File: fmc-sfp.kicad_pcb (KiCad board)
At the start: 2 copper layers, 89.5 x 70 mm, 41 parts, among them J1 ASP-134604-01, J2 SFP+, J3 SFP+, J4 132134, J5 132134, J6 132134, J7 132134, U1 MAX9113EKA_TT, U2 MAX9113EKA_TT

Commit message: update after Phil review
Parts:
- removed J3: SFP+, Connector:Connector_SFP_and_Cage
- removed R10, R15, R16, R17, R18, R7, R8, R9: 10k, Resistor_SMD:R_0603_1608Metric
- added G***: LOGO, project:Microridge_logo, B.Cu at (118.2, 78.8)
- added J8: SFPK-SL, project:SAMTEC_SFPK-SL, B.Cu at (104.0, 60.1)
- J2: value SFP+ -> SFPK-SL; footprint Connector:Connector_SFP_and_Cage -> project:SAMTEC_SFPK-SL
- moved J2 37.5 mm to (103.7, 97.2), turned to -90 degrees
- moved J4 3.95 mm to (89.2, 54.2)
- moved J7 3.95 mm to (89.1, 109.7)
- moved J6 1.05 mm to (75.6, 109.8)
- moved J5 1.05 mm to (75.8, 54.2)
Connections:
- J2 pad 10: unconnected-(J2-VeeR-Pad10)_1 -> GND
- J2 pad 11: unconnected-(J2-VeeR-Pad10)_0 -> GND
- J2 pad 12: /lvds_0_rx_N -> /lvds_1_rx_N
- J2 pad 13: /lvds_0_rx_P -> /lvds_1_rx_P
- J2 pad 14: unconnected-(J2-VeeR-Pad10) -> GND
- J2 pad 15: unconnected-(J2-VccR-Pad15) -> /SPF1/VccR
- J2 pad 16: unconnected-(J2-VccT-Pad16) -> /SPF1/VccT
- J2 pad 17: unconnected-(J2-VeeT-Pad1)_0 -> GND
- J2 pad 18: /lvds_0_tx_P -> /lvds_1_tx_P
- J2 pad 19: /lvds_0_tx_N -> /lvds_1_tx_N
- J2 pad 20: unconnected-(J2-VeeT-Pad1)_1 -> GND
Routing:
- net VSS: track 83.2 -> 55.6 mm, vias 5 -> 4
- net GND: track 8.23 -> 15.2 mm
- net /RX0: track 16.6 -> 18.2 mm
- net /RX1: track 10.1 -> 11.7 mm
- net /lvds_0_tx_N: track 37.9 -> 36.6 mm
- net /lvds_0_tx_P: track 39.5 -> 38.1 mm
- net /lvds_1_tx_P: track 51.1 -> 49.8 mm
- net /lvds_1_tx_N: track 49.9 -> 48.5 mm

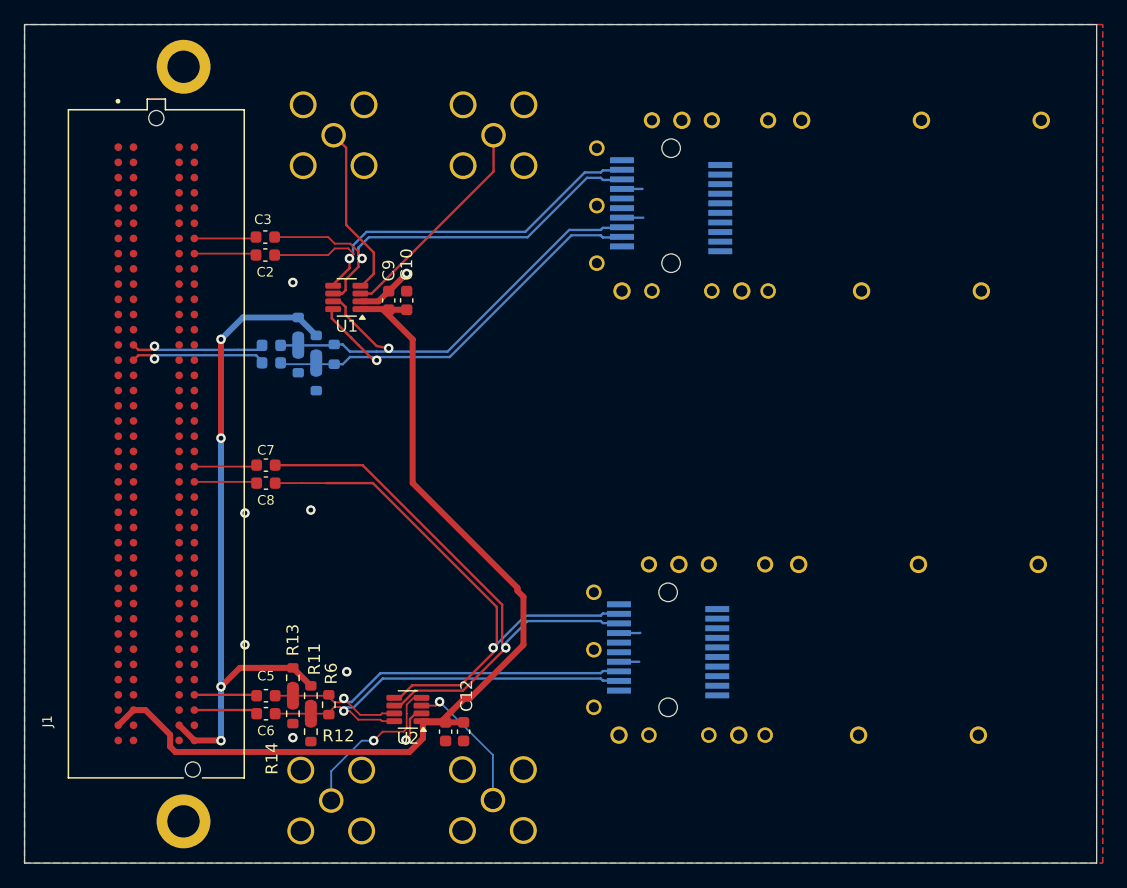
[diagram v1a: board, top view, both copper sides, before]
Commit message: Minor tweaks to sfp cage position, fix silkscreen s/RX/TX/
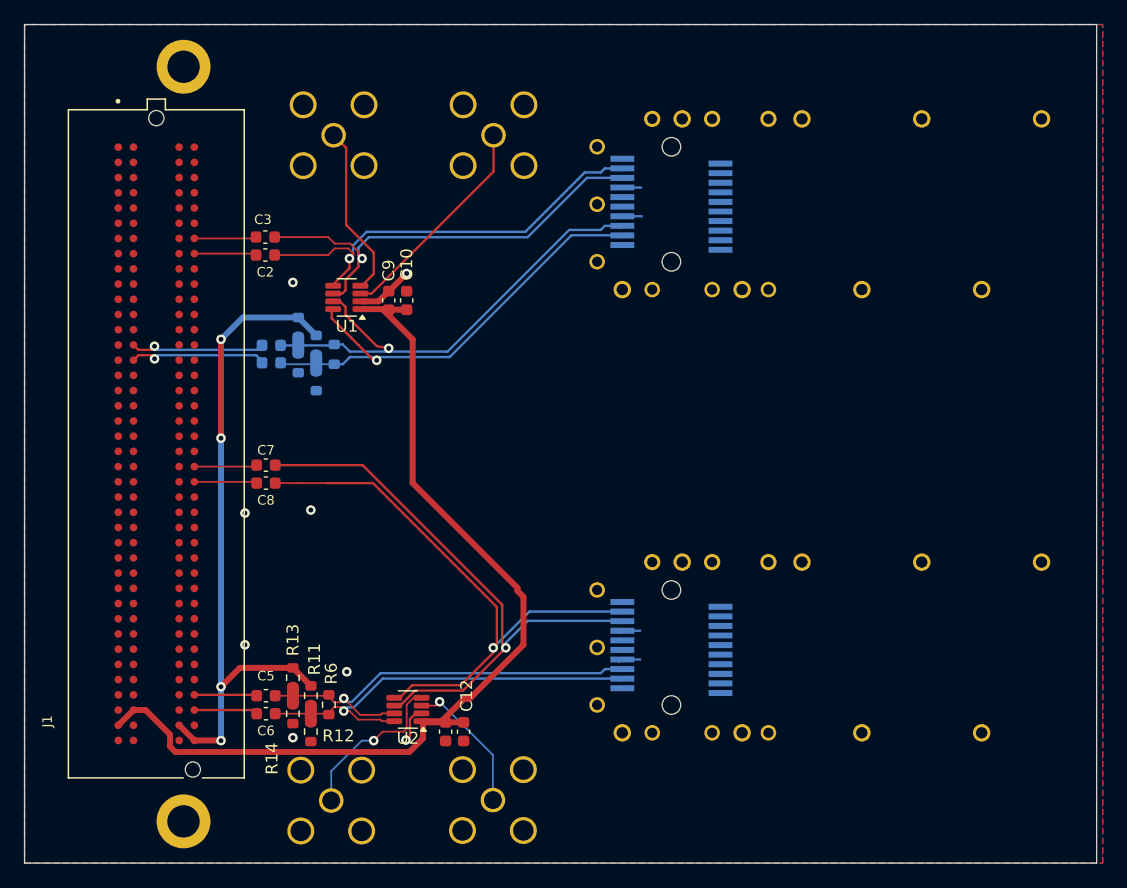
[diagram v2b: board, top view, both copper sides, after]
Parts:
- moved J2 0.34 mm to (104.0, 97.0)
- moved J8 0.12 mm to (104.0, 60.0)
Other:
- board text added: "TX1"

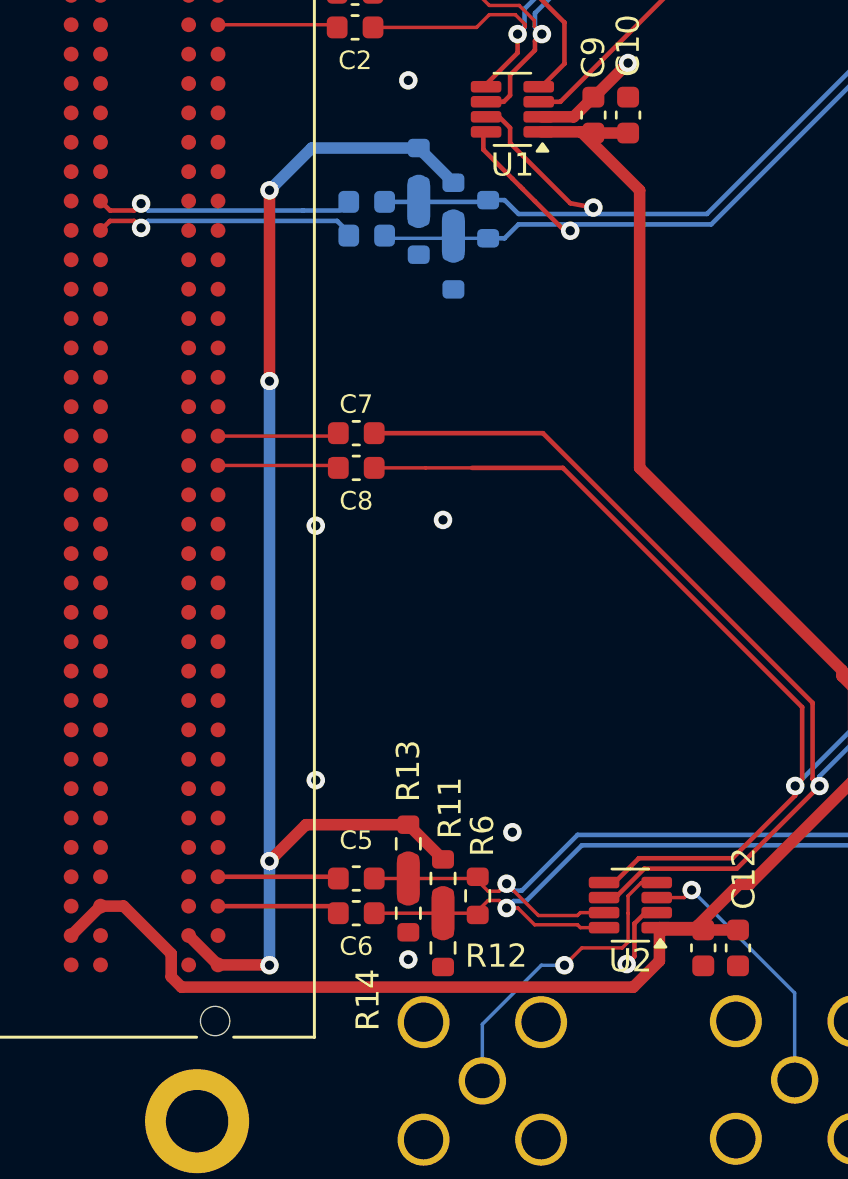
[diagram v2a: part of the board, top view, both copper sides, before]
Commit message: move termination resistors to FPGA side of capacitors
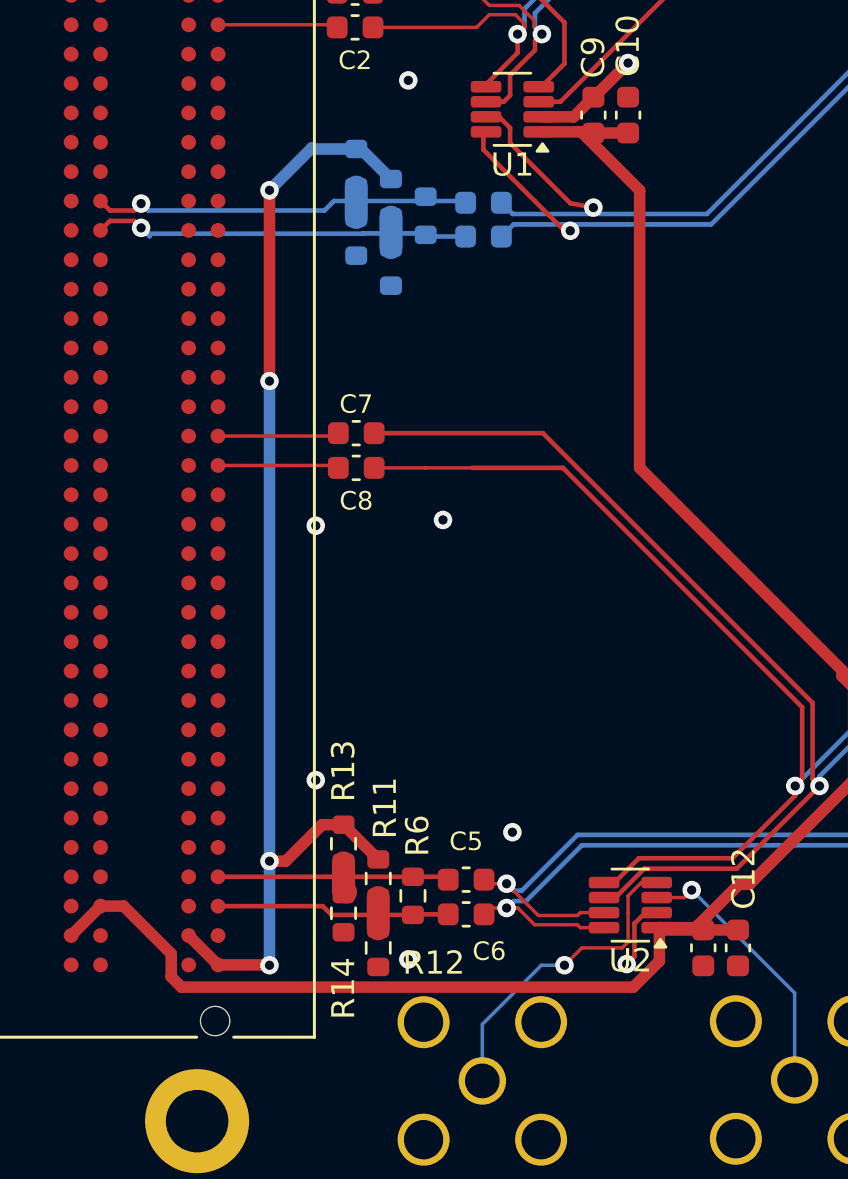
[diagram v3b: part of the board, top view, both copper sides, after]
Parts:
- moved C1 5.05 mm to (75.7, 73.3)
- moved C4 5.05 mm to (75.7, 71.8)
- moved C5 4.75 mm to (74.9, 101.1)
- moved C6 4.75 mm to (74.9, 102.6)
- moved R11 2.80 mm to (71.1, 101.0)
- moved R12 2.80 mm to (71.1, 104.0)
- moved R13 2.80 mm to (69.6, 99.5)
- moved R14 2.80 mm to (69.6, 102.5)
- moved R6 2.80 mm to (72.6, 101.8)
- moved R4 2.70 mm to (71.7, 71.6)
- moved R5 2.70 mm to (71.7, 74.6)
- moved R1 2.70 mm to (73.2, 72.4)
- moved R3 2.70 mm to (70.2, 73.3)
- moved R2 2.70 mm to (70.2, 70.3)
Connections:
- R1 pad 1: /lvds_0_rx_N -> /FMC_LA09_N
- R1 pad 2: /lvds_0_rx_P -> /FMC_LA09_P
- R11 pad 2: /lvds_1_rx_N -> /FMC_LA32_N
- R12 pad 1: /lvds_1_rx_N -> /FMC_LA32_N
- R13 pad 2: /lvds_1_rx_P -> /FMC_LA32_P
- R14 pad 1: /lvds_1_rx_P -> /FMC_LA32_P
- R2 pad 2: /lvds_0_rx_P -> /FMC_LA09_P
- R3 pad 1: /lvds_0_rx_P -> /FMC_LA09_P
- R4 pad 2: /lvds_0_rx_N -> /FMC_LA09_N
- R5 pad 1: /lvds_0_rx_N -> /FMC_LA09_N
- R6 pad 1: /lvds_1_rx_N -> /FMC_LA32_N
- R6 pad 2: /lvds_1_rx_P -> /FMC_LA32_P
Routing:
- net /FMC_LA09_N: track 11.5 -> 18.2 mm
- net /lvds_0_rx_P: track 41.4 -> 34.7 mm
- net /lvds_0_rx_N: track 40.9 -> 34.5 mm
- net /lvds_1_rx_P: track 36.7 -> 30.2 mm
- net /lvds_1_rx_N: track 36.3 -> 29.9 mm
- net /FMC_LA09_P: track 11.3 -> 17.7 mm
- net /FMC_LA32_N: track 5.30 -> 11.6 mm
- net /FMC_LA32_P: track 5.72 -> 11.6 mm
- net VSS: track 55.6 -> 50.1 mm

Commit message: clean up a trace
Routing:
- net +3V3: track 80.0 -> 79.4 mm
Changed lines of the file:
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@@
 	)
 	(segment
-		(start 59.095 102.225)
-		(end 57.825 103.495)
+		(start 87.15 101.28)
+		(end 90.925 97.505)
 		(width 0.5)
 		(layer "F.Cu")
@@
 	)
 	(segment
-		(start 91.15 92.03)
-		(end 82.4 83.28)
-		(width 0.5)
-		(layer "F.Cu")
-		(net 148)
-	)
-	(segment
-		(start 82.4 83.28)
-		(end 82.4 71.28)
-		(width 0.5)
-		(layer "F.Cu")
-		(net 148)
-	)
-	(segment
-		(start 91.65 96.78)
-		(end 91.65 92.78)
-		(width 0.5)
-		(layer "F.Cu")
-		(net 148)
-	)
-	(segment
-		(start 82.4 71.28)
-		(end 79.875 68.755)
+		(start 59.095 102.225)
+		(end 57.825 103.495)
 		(width 0.5)
 		(layer "F.Cu")
@@
 	)
 	(segment
-		(start 59.095 102.225)
-		(end 60.095 102.225)
+		(start 84.825 103.155)
+		(end 86.7 101.28)
 		(width 0.5)
 		(layer "F.Cu")
@@
 	)
 	(segment
-		(start 79.875 68.755)
-		(end 78.155 68.755)
+		(start 59.095 102.225)
+		(end 60.095 102.225)
 		(width 0.5)
 		(layer "F.Cu")
@@
 	)
 	(segment
-		(start 86.7 101.28)
-		(end 87.15 101.28)
-		(width 0.5)
-		(layer "F.Cu")
-		(net 148)
-	)
-	(segment
-		(start 91.65 92.78)
-		(end 91.15 92.28)
-		(width 0.5)
-		(layer "F.Cu")
-		(net 148)
-	)
-	(segment
 		(start 62.15 104.28)
 		(end 62.15 105.28)
-		(width 0.5)
-		(layer "F.Cu")
-		(net 148)
-	)
-	(segment
-		(start 84.825 103.155)
-		(end 86.7 101.28)
 		(width 0.5)
 		(layer "F.Cu")
@@
 	)
 	(segment
-		(start 83.255 103.155)
-		(end 84.825 103.155)
+		(start 90.925 97.505)
+		(end 90.925 96.719339)
 		(width 0.5)
 		(layer "F.Cu")
@@
 	)
 	(segment
+		(start 86.7 101.28)
+		(end 87.15 101.28)
+		(width 0.5)
+		(layer "F.Cu")
+		(net 148)
+	)
+	(segment
+		(start 90.9 79.78)
+		(end 79.875 68.755)
+		(width 0.5)
+		(layer "F.Cu")
+		(net 148)
+	)
+	(segment
+		(start 90.925 96.719339)
+		(end 90.9 96.694339)
+		(width 0.5)
+		(layer "F.Cu")
+		(net 148)
+	)
+	(segment
 		(start 60.095 102.225)
 		(end 62.15 104.28)
@@
 	)
 	(segment
-		(start 91.15 92.28)
-		(end 91.15 92.03)
+		(start 90.9 96.694339)
+		(end 90.9 79.78)
+		(width 0.5)
+		(layer "F.Cu")
+		(net 148)
+	)
+	(segment
+		(start 83.255 103.155)
+		(end 84.825 103.155)
+		(width 0.5)
+		(layer "F.Cu")
+		(net 148)
+	)
+	(segment
+		(start 79.875 68.755)
+		(end 78.155 68.755)
 		(width 0.5)
 		(layer "F.Cu")
@@
 		(width 0.5)
 		(layer "F.Cu")
-		(net 148)
-	)
-	(segment
-		(start 87.15 101.28)
-		(end 91.65 96.78)
-		(width 0.5)
-		(layer "F.Cu")

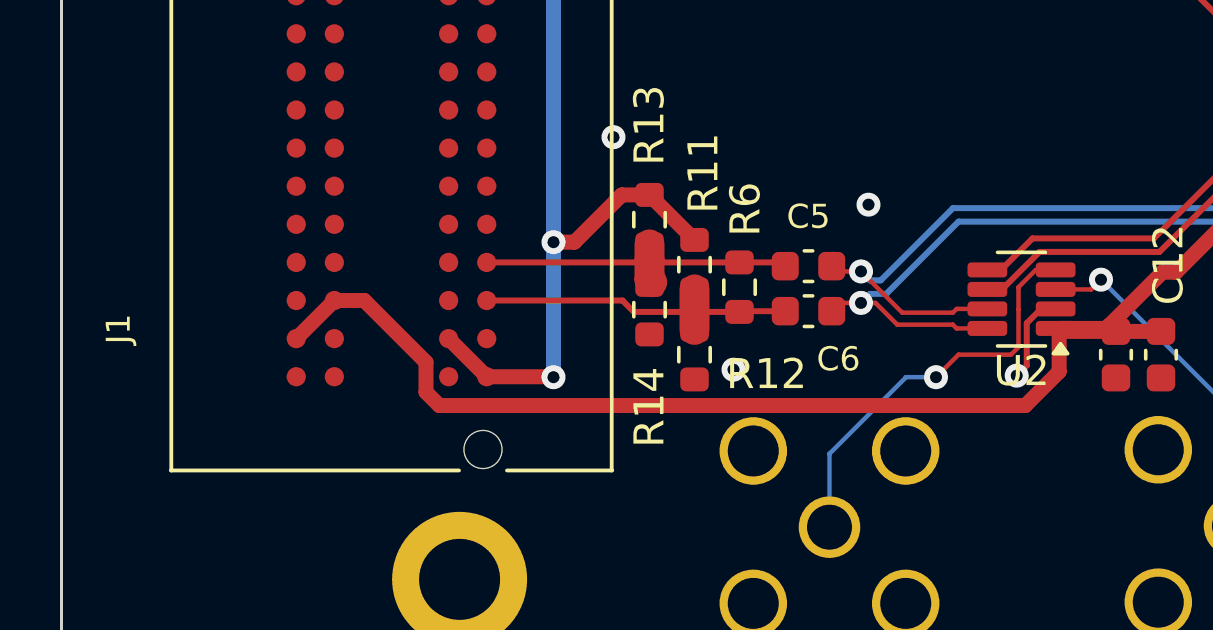
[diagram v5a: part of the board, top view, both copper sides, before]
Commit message: connect all grounds for fmc connector
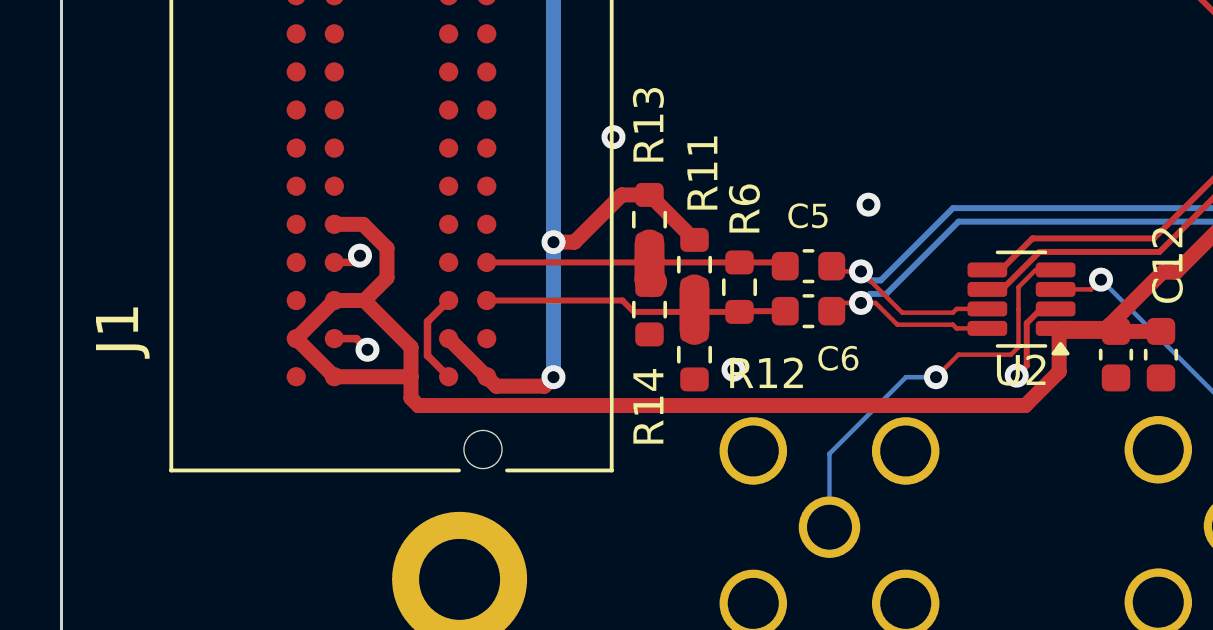
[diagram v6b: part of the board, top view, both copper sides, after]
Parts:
- J1: footprint ASP_134604_01:SAMTEC_ASP-134604-01 -> project:SAMTEC_ASP-134604-01
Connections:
- J1 pad C1: unconnected-(J1-PadC1) -> GND
- J1 pad C12: unconnected-(J1-PadC12) -> GND
- J1 pad C13: unconnected-(J1-PadC13) -> GND
- J1 pad C16: unconnected-(J1-PadC16) -> GND
- J1 pad C17: unconnected-(J1-PadC17) -> GND
- J1 pad C20: unconnected-(J1-PadC20) -> GND
- J1 pad C21: unconnected-(J1-PadC21) -> GND
- J1 pad C24: unconnected-(J1-PadC24) -> GND
- J1 pad C25: unconnected-(J1-PadC25) -> GND
- J1 pad C28: unconnected-(J1-PadC28) -> GND
- J1 pad C29: unconnected-(J1-PadC29) -> GND
- J1 pad C32: unconnected-(J1-PadC32) -> GND
- J1 pad C33: unconnected-(J1-PadC33) -> GND
- J1 pad C36: unconnected-(J1-PadC36) -> GND
- J1 pad C38: unconnected-(J1-PadC38) -> GND
- J1 pad C4: unconnected-(J1-PadC4) -> GND
- J1 pad C40: unconnected-(J1-PadC40) -> GND
- J1 pad C5: unconnected-(J1-PadC5) -> GND
- J1 pad C8: unconnected-(J1-PadC8) -> GND
- J1 pad C9: unconnected-(J1-PadC9) -> GND
- J1 pad D36: unconnected-(J1-PadD36) -> +3V3
- J1 pad D40: unconnected-(J1-PadD40) -> +3V3
- J1 pad G1: unconnected-(J1-PadG1) -> GND
- J1 pad G11: unconnected-(J1-PadG11) -> GND
- J1 pad G14: unconnected-(J1-PadG14) -> GND
- J1 pad G17: unconnected-(J1-PadG17) -> GND
- J1 pad G20: unconnected-(J1-PadG20) -> GND
- J1 pad G23: unconnected-(J1-PadG23) -> GND
- J1 pad G26: unconnected-(J1-PadG26) -> GND
- J1 pad G29: unconnected-(J1-PadG29) -> GND
- J1 pad G32: unconnected-(J1-PadG32) -> GND
- J1 pad G35: unconnected-(J1-PadG35) -> GND
- J1 pad G38: unconnected-(J1-PadG38) -> GND
- J1 pad G4: unconnected-(J1-PadG4) -> GND
- J1 pad G40: unconnected-(J1-PadG40) -> GND
- J1 pad G5: unconnected-(J1-PadG5) -> GND
- J1 pad G8: unconnected-(J1-PadG8) -> GND
- J1 pad H12: unconnected-(J1-PadH12) -> GND
- J1 pad H15: unconnected-(J1-PadH15) -> GND
- J1 pad H18: unconnected-(J1-PadH18) -> GND
- J1 pad H21: unconnected-(J1-PadH21) -> GND
- J1 pad H24: unconnected-(J1-PadH24) -> GND
- J1 pad H27: unconnected-(J1-PadH27) -> GND
- J1 pad H3: unconnected-(J1-PadH3) -> GND
- J1 pad H30: unconnected-(J1-PadH30) -> GND
- J1 pad H33: unconnected-(J1-PadH33) -> GND
- J1 pad H36: unconnected-(J1-PadH36) -> GND
- J1 pad H39: unconnected-(J1-PadH39) -> GND
- J1 pad H6: unconnected-(J1-PadH6) -> GND
- J1 pad H9: unconnected-(J1-PadH9) -> GND
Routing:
- net +3V3: track 79.4 -> 88.3 mm
- net GND: track 15.3 -> 20.6 mm, vias 8 -> 10
